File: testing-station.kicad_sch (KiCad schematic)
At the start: 0 parts

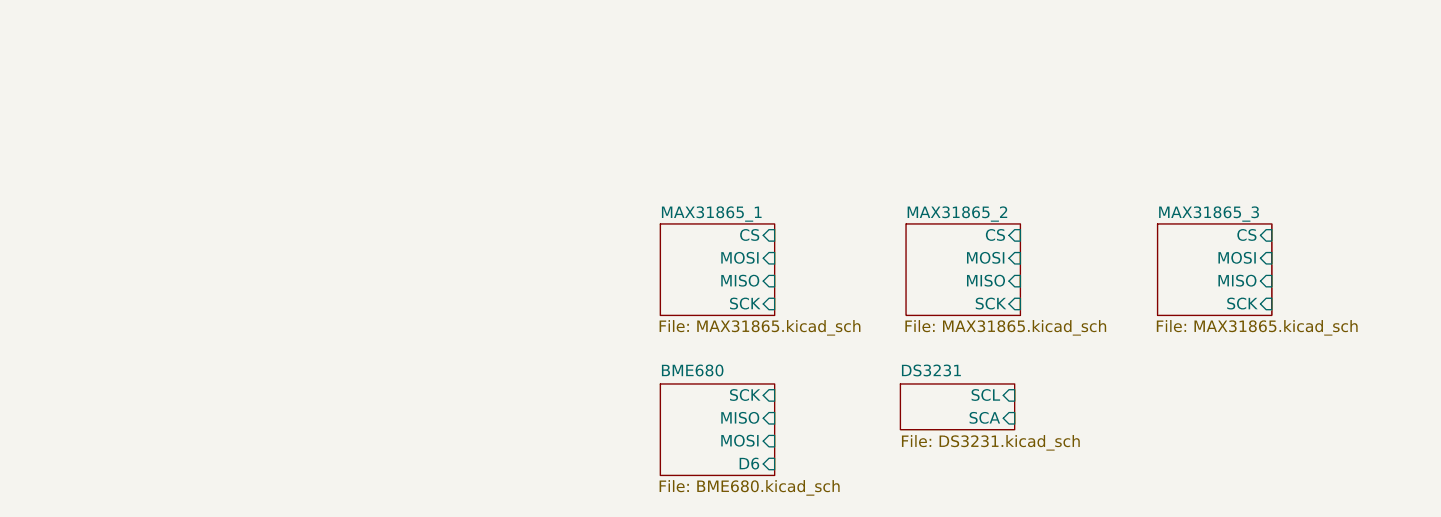
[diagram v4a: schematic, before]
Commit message: added microSD schematic page
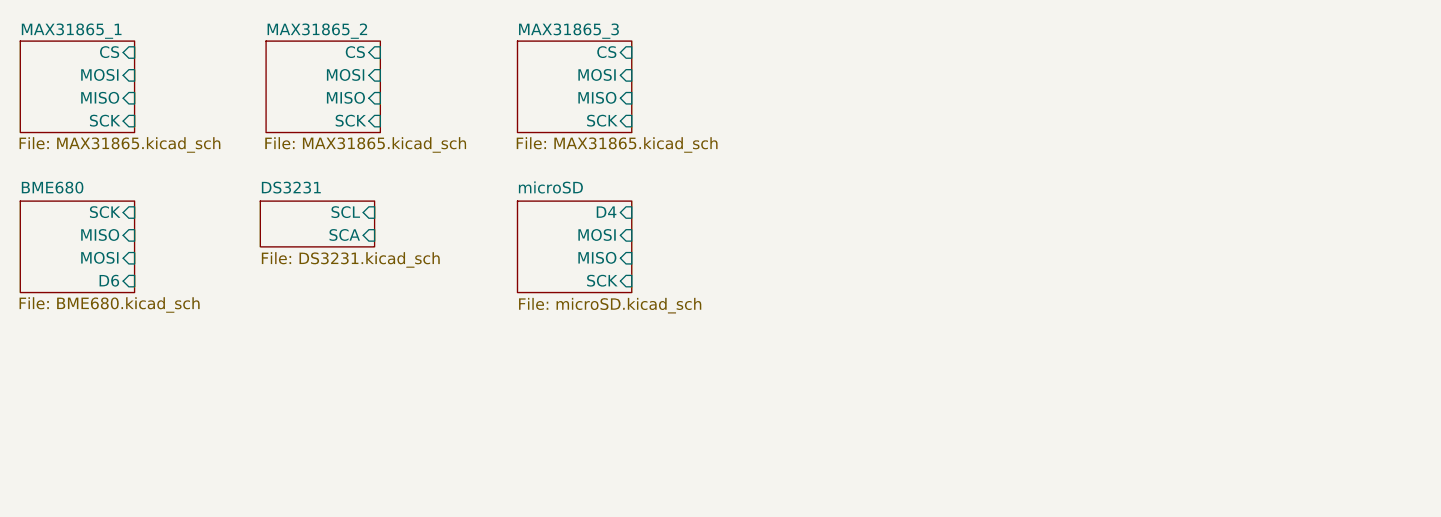
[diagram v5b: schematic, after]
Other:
- added sheet microSD (microSD.kicad_sch)
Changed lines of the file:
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@@
 	(paper "A4")
 	(sheet
-		(at 175.26 68.58)
+		(at 104.14 66.04)
 		(size 12.7 10.16)
+		(fields_autoplaced yes)
+		(stroke
+			(width 0.1524)
+			(type solid)
+		)
+		(fill
+			(color 0 0 0 0.0000)
+		)
+		(property "Sheetname" "microSD"
+			(at 104.14 65.3284 0)
+			(effects
+				(font
+					(size 1.27 1.27)
+				)
+				(justify left bottom)
+			)
+		)
+		(property "Sheetfile" "microSD.kicad_sch"
+			(at 104.14 76.7846 0)
+			(effects
+				(font
+					(size 1.27 1.27)
+				)
+				(justify left top)
+			)
+		)
+		(pin "D4" input
+			(at 116.84 67.31 0)
+			(effects
+				(font
+					(size 1.27 1.27)
+				)
+				(justify right)
+			)
+		)
+		(pin "SCK" input
+			(at 116.84 74.93 0)
+			(effects
+				(font
+					(size 1.27 1.27)
+				)
+				(justify right)
+			)
+		)
+		(pin "MISO" input
+			(at 116.84 72.39 0)
+			(effects
+				(font
+					(size 1.27 1.27)
+				)
+				(justify right)
+			)
+		)
+		(pin "MOSI" input
+			(at 116.84 69.85 0)
+			(effects
+				(font
+					(size 1.27 1.27)
+				)
+				(justify right)
+			)
+		)
+		(instances
+			(project "testing-station"
+				(path "/ed3950ec-e24f-4dd6-b9cc-eca012f1333b"
+					(page "7")
+				)
+			)
+		)
+	)
+	(sheet
+		(at 104.14 48.26)
+		(size 12.7 10.16)
 		(stroke
 			(width 0.1524)
@@
 		)
 		(property "Sheetname" "MAX31865_3"
-			(at 175.26 68.072 0)
+			(at 104.14 47.752 0)
 			(effects
 				(font
@@
 		)
 		(property "Sheetfile" "MAX31865.kicad_sch"
-			(at 175.006 79.248 0)
+			(at 103.886 58.928 0)
 			(effects
 				(font
@@
 		)
 		(pin "SCK" input
-			(at 187.96 77.47 0)
+			(at 116.84 57.15 0)
 			(effects
 				(font
@@
 		)
 		(pin "MISO" input
-			(at 187.96 74.93 0)
+			(at 116.84 54.61 0)
 			(effects
 				(font
@@
 		)
 		(pin "CS" input
-			(at 187.96 69.85 0)
+			(at 116.84 49.53 0)
 			(effects
 				(font
@@
 		)
 		(pin "MOSI" input
-			(at 187.96 72.39 0)
+			(at 116.84 52.07 0)
 			(effects
 				(font
@@
 	)
 	(sheet
-		(at 146.685 86.36)
+		(at 75.565 66.04)
 		(size 12.7 5.08)
 		(fields_autoplaced yes)
@@
 		)
 		(property "Sheetname" "DS3231"
-			(at 146.685 85.6484 0)
+			(at 75.565 65.3284 0)
 			(effects
 				(font
@@
 		)
 		(property "Sheetfile" "DS3231.kicad_sch"
-			(at 146.685 92.0246 0)
+			(at 75.565 71.7046 0)
 			(effects
 				(font
@@
 		)
 		(pin "SCL" input
-			(at 159.385 87.63 0)
+			(at 88.265 67.31 0)
 			(effects
 				(font
@@
 		)
 		(pin "SCA" input
-			(at 159.385 90.17 0)
+			(at 88.265 69.85 0)
 			(effects
 				(font
@@
 	)
 	(sheet
-		(at 120.015 86.36)
+		(at 48.895 66.04)
 		(size 12.7 10.16)
 		(stroke
@@
 		)
 		(property "Sheetname" "BME680"
-			(at 120.015 85.6484 0)
+			(at 48.895 65.3284 0)
 			(effects
 				(font
@@
 		)
 		(property "Sheetfile" "BME680.kicad_sch"
-			(at 119.761 97.028 0)
+			(at 48.641 76.708 0)
 			(effects
 				(font
@@
 		)
 		(pin "MOSI" input
-			(at 132.715 92.71 0)
+			(at 61.595 72.39 0)
 			(effects
 				(font
@@
 		)
 		(pin "D6" input
-			(at 132.715 95.25 0)
+			(at 61.595 74.93 0)
 			(effects
 				(font
@@
 		)
 		(pin "MISO" input
-			(at 132.715 90.17 0)
+			(at 61.595 69.85 0)
 			(effects
 				(font
@@
 		)
 		(pin "SCK" input
-			(at 132.715 87.63 0)
+			(at 61.595 67.31 0)
 			(effects
 				(font
@@
 	)
 	(sheet
-		(at 120.015 68.58)
+		(at 48.895 48.26)
 		(size 12.7 10.16)
 		(stroke
@@
 		)
 		(property "Sheetname" "MAX31865_1"
-			(at 120.015 68.072 0)
+			(at 48.895 47.752 0)
 			(effects
 				(font
@@
 		)
 		(property "Sheetfile" "MAX31865.kicad_sch"
-			(at 119.761 79.248 0)
+			(at 48.641 58.928 0)
 			(effects
 				(font
@@
 		)
 		(pin "SCK" input
-			(at 132.715 77.47 0)
+			(at 61.595 57.15 0)
 			(effects
 				(font
@@
 		)
 		(pin "MISO" input
-			(at 132.715 74.93 0)
+			(at 61.595 54.61 0)
 			(effects
 				(font
@@
 		)
 		(pin "CS" input
-			(at 132.715 69.85 0)
+			(at 61.595 49.53 0)
 			(effects
 				(font
@@
 		)
 		(pin "MOSI" input
-			(at 132.715 72.39 0)
+			(at 61.595 52.07 0)
 			(effects
 				(font
@@
 	)
 	(sheet
-		(at 147.32 68.58)
+		(at 76.2 48.26)
 		(size 12.7 10.16)
 		(stroke
@@
 		)
 		(property "Sheetname" "MAX31865_2"
-			(at 147.32 68.072 0)
+			(at 76.2 47.752 0)
 			(effects
 				(font
@@
 		)
 		(property "Sheetfile" "MAX31865.kicad_sch"
-			(at 147.066 79.248 0)
+			(at 75.946 58.928 0)
 			(effects
 				(font
@@
 		)
 		(pin "SCK" input
-			(at 160.02 77.47 0)
+			(at 88.9 57.15 0)
 			(effects
 				(font
@@
 		)
 		(pin "MISO" input
-			(at 160.02 74.93 0)
+			(at 88.9 54.61 0)
 			(effects
 				(font
@@
 		)
 		(pin "CS" input
-			(at 160.02 69.85 0)
+			(at 88.9 49.53 0)
 			(effects
 				(font
@@
 		)
 		(pin "MOSI" input
-			(at 160.02 72.39 0)
-			(effects
-				(font
+			(at 88.9 52.07 0)
+			(effects
+				(font

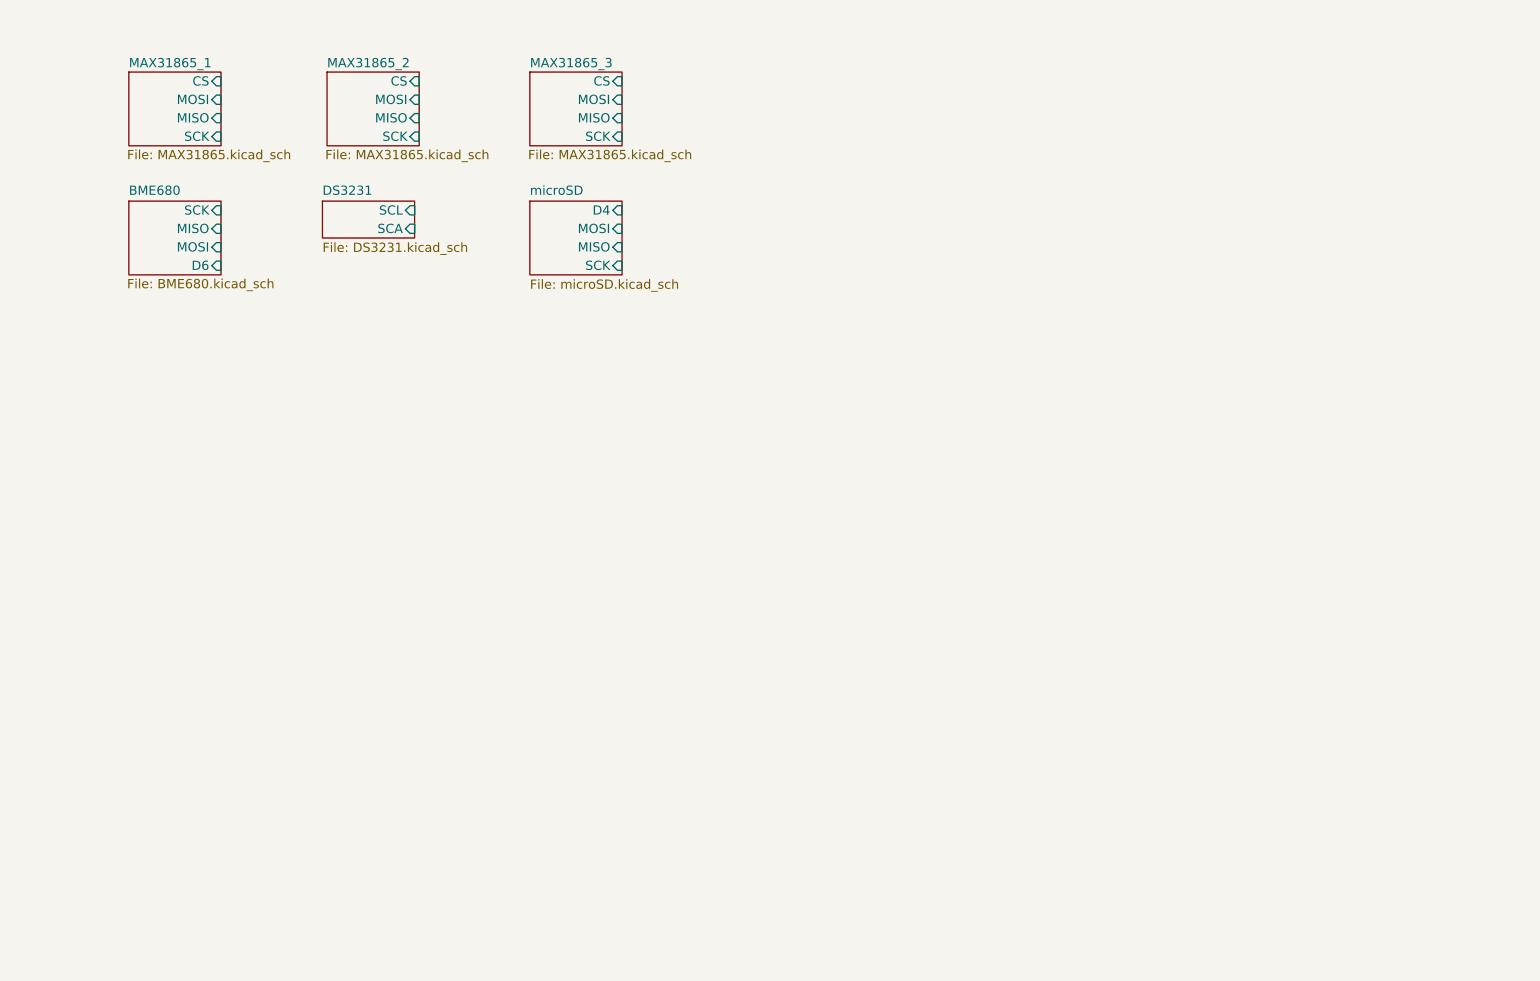
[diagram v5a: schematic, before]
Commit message: added Arduino UNO R4 in root sheet
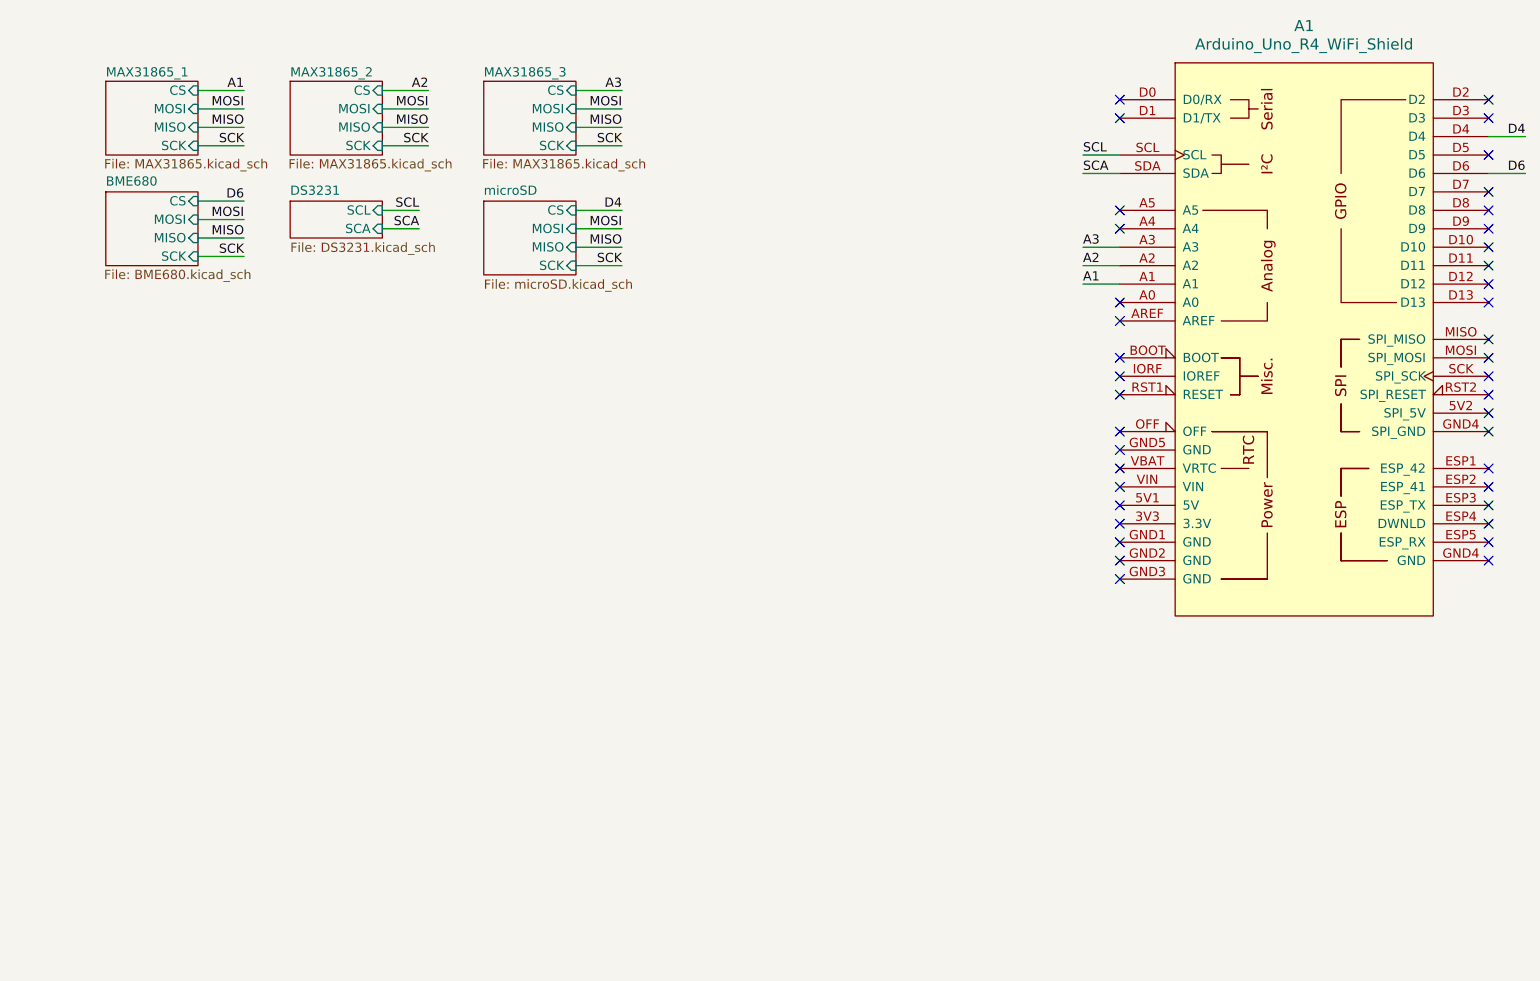
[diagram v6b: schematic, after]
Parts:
- added A1: Arduino_Uno_R4_WiFi_Shield, PCM_arduino-library:Arduino_Uno_R4_WiFi_Shield, symbol PCM_arduino-library:Arduino_Uno_R4_WiFi_Shield
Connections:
- new net A1: A1.A1
- new net A2: A1.A2
- new net A3: A1.A3
- new net D4: A1.D4
- new net D6: A1.D6
- new net SCA: A1.SDA
- new net SCL: A1.SCL
- no-connect marks 0 -> 40
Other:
- sheet BME680 ports: added CS; removed D6
- sheet microSD ports: added CS; removed D4

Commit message: added pyrano, anemo, AM2315C, power supply, LEDs, switch and FPC connector in schematic
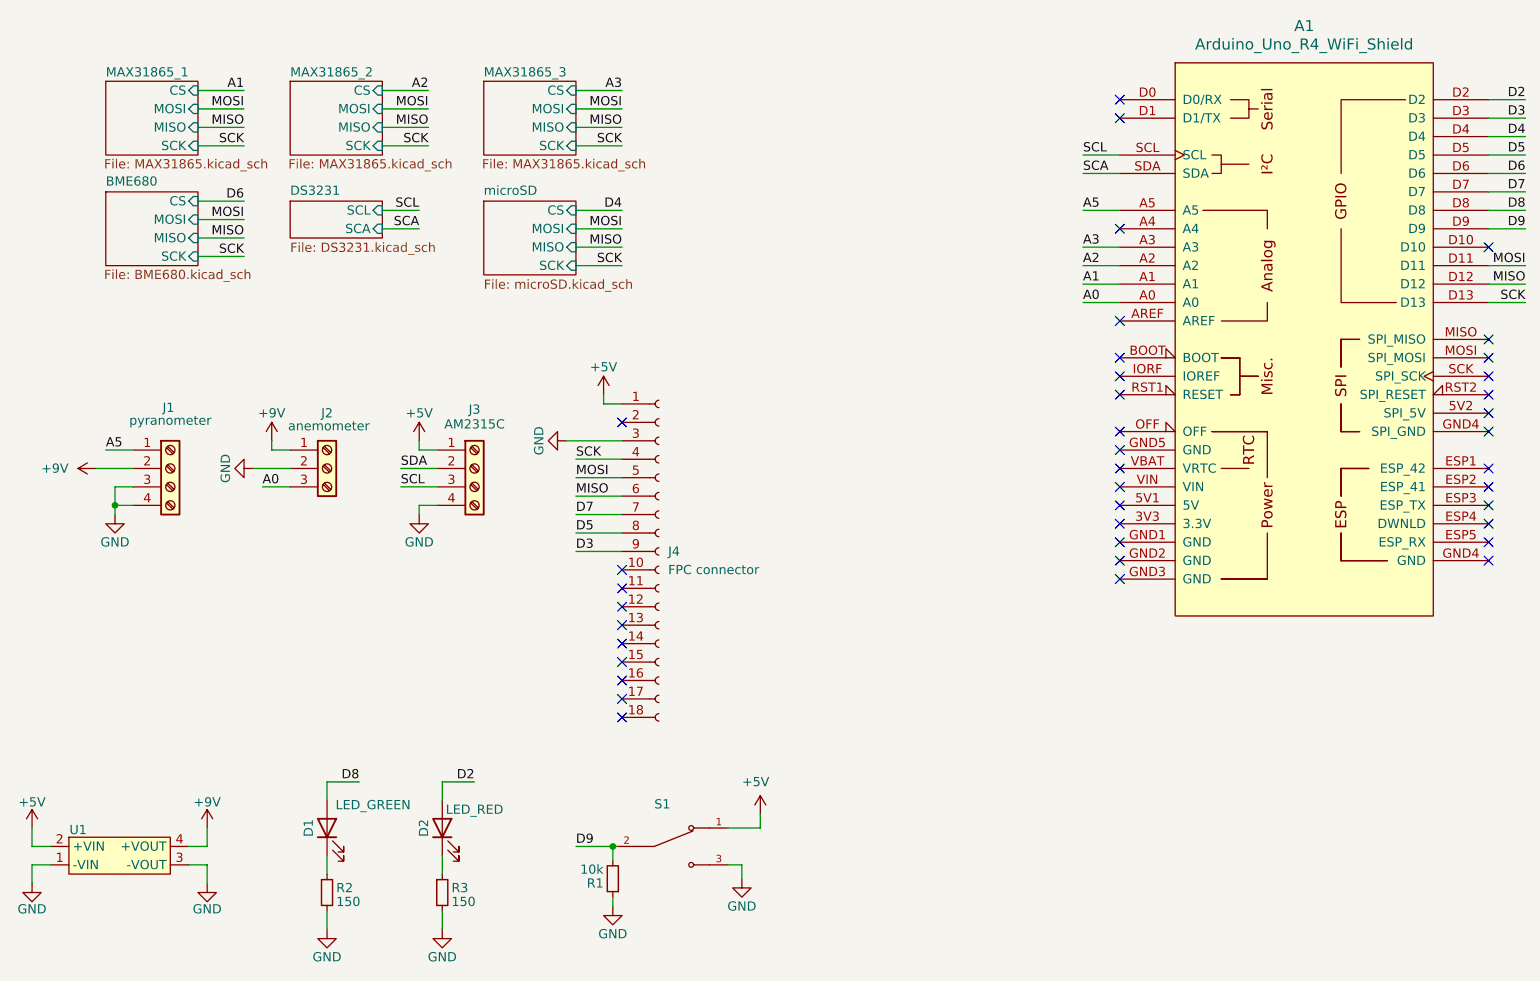
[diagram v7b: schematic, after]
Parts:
- added D1: LED_GREEN, LED_SMD:LED_1206_3216Metric_Pad1.42x1.75mm_HandSolder, symbol Device:LED
- added D2: LED_RED, LED_SMD:LED_1206_3216Metric_Pad1.42x1.75mm_HandSolder, symbol Device:LED
- added J1: pyranometer, custom_components:screw_terminal_4pin, symbol Connector:Screw_Terminal_01x04
- added J2: anemometer, custom_components:screw_terminal_3pin, symbol Connector:Screw_Terminal_01x03
- added J3: AM2315C, custom_components:screw_terminal_4pin, symbol Connector:Screw_Terminal_01x04
- added J4: FPC connector, external_footprints:XF2M-1815-1A, symbol Connector:Conn_01x18_Socket
- added R1: 10k, Resistor_SMD:R_1206_3216Metric_Pad1.30x1.75mm_HandSolder, symbol Device:R_Small
- added R2, R3: 150, Resistor_SMD:R_1206_3216Metric_Pad1.30x1.75mm_HandSolder, symbol Device:R_Small
- added S1: 500SSP1S2M2QEA, 500SSP1S2M2QEA:SW_500SSP1S2M2QEA, symbol 500SSP1S2M2QEA:500SSP1S2M2QEA
- added U1: TBA_1-0519, TBA_1-0519:CONV_TBA_1-0519, symbol external_symbols:PSU
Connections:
- net MISO: now also A1.D12, J4.6 (Pin_6)
- net MOSI: now also A1.D11, J4.5 (Pin_5)
- net SCK: now also A1.D13, J4.4 (Pin_4)
- net SCL: now also J3.3 (Pin_3)
- net A0: now reaches A1.A0
- net A0: now also J2.3 (Pin_3)
- net A5: now reaches A1.A5
- net A5: now also J1.1 (Pin_1)
- net D2: now reaches A1.D2
- net D2: now also D2.2 (A)
- net D3: now reaches A1.D3
- net D3: now also J4.9 (Pin_9)
- net D5: now reaches A1.D5
- net D5: now also J4.8 (Pin_8)
- net D7: now reaches A1.D7
- net D7: now also J4.7 (Pin_7)
- net D8: now reaches A1.D8
- net D8: now also D1.2 (A)
- net D9: now reaches A1.D9
- net D9: now also R1.2, S1.2
- new net: D1.1 (K), R2.1
- new net: D2.1 (K), R3.1
- new net +5V: J3.1 (Pin_1), J4.1 (Pin_1), S1.1, U1.2 (+VIN)
- new net +9V: J1.2 (Pin_2), J2.1 (Pin_1), U1.4 (+VOUT)
- new net GND: J1.3 (Pin_3), J1.4 (Pin_4), J2.2 (Pin_2), J3.4 (Pin_4), J4.3 (Pin_3), R1.1, R2.2, R3.2, S1.3, U1.1 (-VIN), U1.3 (-VOUT)
- new net SDA: J3.2 (Pin_2)
- no-connect marks 40 -> 39
